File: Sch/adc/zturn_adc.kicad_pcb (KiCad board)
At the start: 4 copper layers, 91.5 x 80 mm, 118 parts, among them CN1 SMA, CN2 SMA, CN3 AudioJack, J1 JP4, J2 Header5, J3 JP2, J4 JP2, J5 JP2, J6 JP2, P1 CONN_02X40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

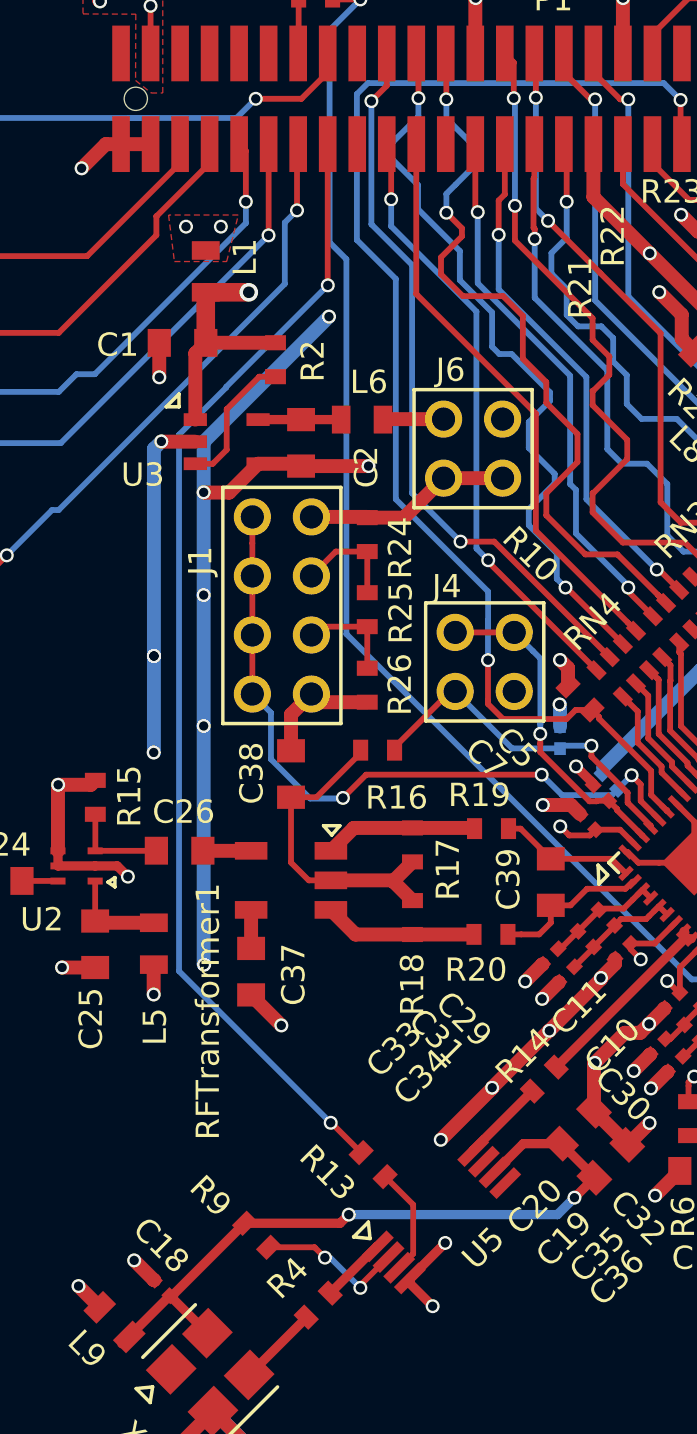
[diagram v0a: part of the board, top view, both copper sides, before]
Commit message: Modify footprint for CDCLVC1102. Changed width of ADC_CLK.
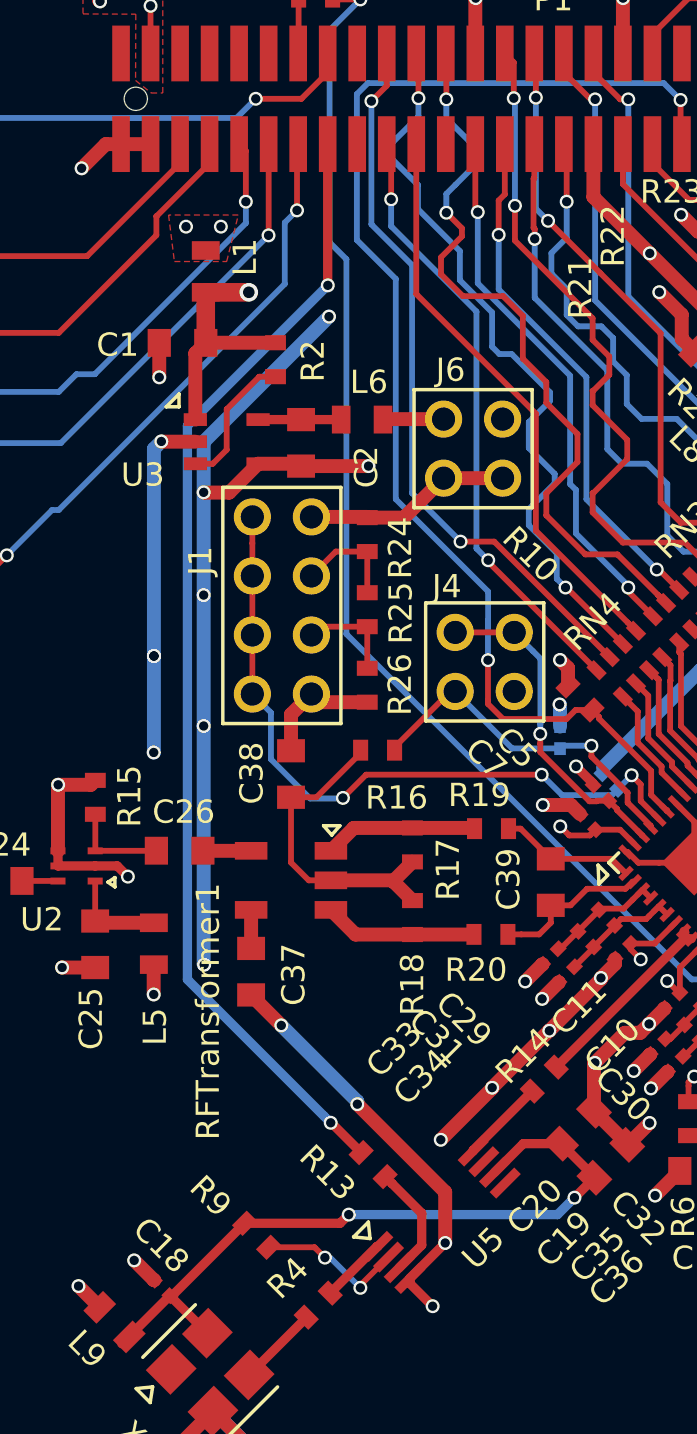
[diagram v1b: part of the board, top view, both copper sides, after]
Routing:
- net GND: track 282.3 -> 294.6 mm, vias 67 -> 68
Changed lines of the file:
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@@
     (thickness 1.6)
     (drawings 7)
-    (tracks 1227)
+    (tracks 1232)
     (zones 0)
     (modules 118)
@@
   (layers
     (0 F.Cu signal)
-    (1 In1.Cu power)
-    (2 In2.Cu power)
+    (1 In1.Cu power hide)
+    (2 In2.Cu power hide)
     (31 B.Cu signal)
     (32 B.Adhes user)
@@
     (add_net /RF_in/VCMA)
     (add_net /RF_in/VCMB)
-    (add_net ADC_CLK)
     (add_net BCLK)
     (add_net DACIN)
@@
     (add_net "Net-(P1-Pad78)")
     (add_net "Net-(P1-Pad79)")
-    (add_net "Net-(R13-Pad2)")
     (add_net "Net-(R2-Pad2)")
     (add_net "Net-(R23-Pad1)")
@@
     (uvia_drill 0.1)
     (add_net /RF_in/CLK40M)
+    (add_net ADC_CLK)
     (add_net "Net-(C12-Pad1)")
     (add_net "Net-(C18-Pad1)")
     (add_net "Net-(C2-Pad1)")
     (add_net "Net-(C49-Pad1)")
+    (add_net "Net-(R13-Pad2)")
     (add_net "Net-(R14-Pad2)")
     (add_net "Net-(R4-Pad1)")
@@
       (net 16 "Net-(C18-Pad1)"))
   )
-  (module adc_lib:CDCLVC1102 (layer F.Cu)
-    (at 129.991951 111.505513 45)
-    (attr smd)
-    (fp_text reference U5 (at 0.254 2.286 45) (layer F.SilkS)
-      (effects (font (size 1 1) (thickness 0.15)))
-    )
-    (fp_text value CDCLVC1102 (at 0.2 -3.45 45) (layer F.Fab)
-      (effects (font (size 1 1) (thickness 0.15)))
-    )
-    (fp_line (start -3.35 -2) (end -2.9 -1.45) (layer F.SilkS) (width 0.15))
-    (fp_line (start -2.45 -2) (end -3.35 -2) (layer F.SilkS) (width 0.15))
-    (fp_line (start -2.9 -1.45) (end -2.45 -2) (layer F.SilkS) (width 0.15))
-    (pad 1 smd rect (at -2.9 -0.975 45) (size 1.5 0.45) (layers F.Cu F.Paste F.Mask)
-      (net 108 "Net-(R4-Pad1)"))
-    (pad 2 smd rect (at -2.9 -0.325 45) (size 1.5 0.45) (layers F.Cu F.Paste F.Mask)
-      (net 110 "Net-(R9-Pad2)"))
-    (pad 3 smd rect (at -2.9 0.325 45) (size 1.5 0.45) (layers F.Cu F.Paste F.Mask)
-      (net 113 "Net-(R13-Pad2)"))
-    (pad 4 smd rect (at -2.9 0.975 45) (size 1.5 0.45) (layers F.Cu F.Paste F.Mask)
-      (net 2 GND))
-    (pad 5 smd rect (at 2.9 0.975 45) (size 1.5 0.45) (layers F.Cu F.Paste F.Mask)
-      (net 158 "Net-(U5-Pad5)"))
-    (pad 6 smd rect (at 2.9 0.325 45) (size 1.5 0.45) (layers F.Cu F.Paste F.Mask)
-      (net 16 "Net-(C18-Pad1)"))
-    (pad 7 smd rect (at 2.9 -0.325 45) (size 1.5 0.45) (layers F.Cu F.Paste F.Mask)
-      (net 159 "Net-(U5-Pad7)"))
-    (pad 8 smd rect (at 2.9 -0.975 45) (size 1.5 0.45) (layers F.Cu F.Paste F.Mask)
-      (net 114 "Net-(R14-Pad2)"))
-  )
   (module adc_lib:MABAES0060 (layer F.Cu)
     (at 123.517281 97.121151 270)
@@
       (net 3 "Net-(C2-Pad1)"))
   )
+  (module adc_lib:CDCLVC1102 (layer F.Cu)
+    (at 129.991951 111.505513 45)
+    (attr smd)
+    (fp_text reference U5 (at 0.254 2.286 45) (layer F.SilkS)
+      (effects (font (size 1 1) (thickness 0.15)))
+    )
+    (fp_text value CDCLVC1102 (at 0.2 -3.45 45) (layer F.Fab)
+      (effects (font (size 1 1) (thickness 0.15)))
+    )
+    (fp_line (start -3.35 -2) (end -2.9 -1.45) (layer F.SilkS) (width 0.15))
+    (fp_line (start -2.45 -2) (end -3.35 -2) (layer F.SilkS) (width 0.15))
+    (fp_line (start -2.9 -1.45) (end -2.45 -2) (layer F.SilkS) (width 0.15))
+    (pad 1 smd rect (at -2.9 -0.975 45) (size 1.5 0.4) (layers F.Cu F.Paste F.Mask)
+      (net 108 "Net-(R4-Pad1)"))
+    (pad 2 smd rect (at -2.9 -0.325 45) (size 1.5 0.4) (layers F.Cu F.Paste F.Mask)
+      (net 110 "Net-(R9-Pad2)"))
+    (pad 3 smd rect (at -2.9 0.325 45) (size 1.5 0.4) (layers F.Cu F.Paste F.Mask)
+      (net 113 "Net-(R13-Pad2)"))
+    (pad 4 smd rect (at -2.9 0.975 45) (size 1.5 0.4) (layers F.Cu F.Paste F.Mask)
+      (net 2 GND))
+    (pad 5 smd rect (at 2.9 0.975 45) (size 1.5 0.4) (layers F.Cu F.Paste F.Mask)
+      (net 158 "Net-(U5-Pad5)"))
+    (pad 6 smd rect (at 2.9 0.325 45) (size 1.5 0.4) (layers F.Cu F.Paste F.Mask)
+      (net 16 "Net-(C18-Pad1)"))
+    (pad 7 smd rect (at 2.9 -0.325 45) (size 1.5 0.4) (layers F.Cu F.Paste F.Mask)
+      (net 159 "Net-(U5-Pad7)"))
+    (pad 8 smd rect (at 2.9 -0.975 45) (size 1.5 0.4) (layers F.Cu F.Paste F.Mask)
+      (net 114 "Net-(R14-Pad2)"))
+  )
   (dimension 80 (width 0.3) (layer Dwgs.User)
     (gr_text "80.000 mm" (at 181.85 95 270) (layer Dwgs.User)
@@
   (segment (start 149.455065 96.833313) (end 150.360876 97.739124) (width 0.25) (layer F.Cu) (net 1))
   (segment (start 122.845 74) (end 122.85 73.995) (width 0.25) (layer F.Cu) (net 1))
+  (segment (start 126.37 106.75) (end 126.37 106.63) (width 0.6) (layer B.Cu) (net 2))
+  (segment (start 126.37 106.63) (end 123.1 103.36) (width 0.6) (layer B.Cu) (net 2))
+  (segment (start 130.15 112.72) (end 130.15 110.53) (width 0.6) (layer F.Cu) (net 2))
+  (segment (start 130.15 110.53) (end 126.37 106.75) (width 0.6) (layer F.Cu) (net 2))
+  (via (at 126.37 106.75) (size 0.6) (drill 0.4) (layers F.Cu B.Cu) (net 2))
   (segment (start 117.62 87.47) (end 117.62 91.61) (width 0.6) (layer B.Cu) (net 2))
   (via (at 117.61 91.62) (size 0.6) (drill 0.4) (layers F.Cu B.Cu) (net 2))
@@
   (segment (start 125.095 62.37) (end 123.965 63.5) (width 0.25) (layer F.Cu) (net 55))
   (segment (start 125.095 61.55) (end 125.095 60.73) (width 0.25) (layer F.Cu) (net 55))
-  (segment (start 125.225 107.55) (end 125.25 107.55) (width 0.25) (layer F.Cu) (net 56))
-  (segment (start 125.25 107.55) (end 126.533812 108.833812) (width 0.25) (layer F.Cu) (net 56))
-  (segment (start 118.7 77.95) (end 118.7 101.025) (width 0.25) (layer B.Cu) (net 56))
-  (segment (start 118.7 101.025) (end 125.225 107.55) (width 0.25) (layer B.Cu) (net 56))
+  (segment (start 125.225 107.55) (end 125.25 107.55) (width 0.4) (layer F.Cu) (net 56))
+  (segment (start 125.25 107.55) (end 126.533812 108.833812) (width 0.4) (layer F.Cu) (net 56))
+  (segment (start 125.1 71.525) (end 119.05999 77.56501) (width 0.4) (layer B.Cu) (net 56))
+  (segment (start 119.05999 77.56501) (end 119.05999 101.38499) (width 0.4) (layer B.Cu) (net 56))
+  (segment (start 119.05999 101.38499) (end 124.925001 107.250001) (width 0.4) (layer B.Cu) (net 56))
+  (segment (start 124.925001 107.250001) (end 125.225 107.55) (width 0.4) (layer B.Cu) (net 56))
+  (segment (start 125.095 65.45) (end 125.095 71.52) (width 0.4) (layer F.Cu) (net 56))
+  (segment (start 125.095 71.52) (end 125.1 71.525) (width 0.4) (layer F.Cu) (net 56))
   (via (at 125.225 107.55) (size 0.6) (drill 0.4) (layers F.Cu B.Cu) (net 56))
-  (segment (start 120.729103 75.920897) (end 118.7 77.95) (width 0.25) (layer B.Cu) (net 56))
-  (segment (start 125.1 71.525) (end 120.729103 75.895897) (width 0.25) (layer B.Cu) (net 56))
-  (segment (start 120.729103 75.895897) (end 120.729103 75.920897) (width 0.25) (layer B.Cu) (net 56))
-  (segment (start 125.095 65.45) (end 125.095 71.52) (width 0.25) (layer F.Cu) (net 56))
-  (segment (start 125.095 71.52) (end 125.1 71.525) (width 0.25) (layer F.Cu) (net 56))
   (via (at 125.1 71.525) (size 0.6) (drill 0.4) (layers F.Cu B.Cu) (net 56))
   (segment (start 130.81 82.55) (end 128.725 80.465) (width 0.25) (layer B.Cu) (net 58))
@@
   (segment (start 134.927557 105.155694) (end 140.450069 99.633182) (width 0.4) (layer F.Cu) (net 112))
   (segment (start 140.450069 99.633182) (end 140.739966 99.633182) (width 0.4) (layer F.Cu) (net 112))
-  (segment (start 127.566188 109.866188) (end 128.772191 111.072191) (width 0.25) (layer F.Cu) (net 113))
-  (segment (start 128.772191 111.072191) (end 128.772191 113.184892) (width 0.25) (layer F.Cu) (net 113))
-  (segment (start 128.772191 113.184892) (end 128.171151 113.785932) (width 0.25) (layer F.Cu) (net 113))
+  (segment (start 128.171151 113.785932) (end 129.14 112.817083) (width 0.4) (layer F.Cu) (net 113))
+  (segment (start 129.14 112.817083) (end 129.14 111.44) (width 0.4) (layer F.Cu) (net 113))
+  (segment (start 129.14 111.44) (end 127.866708 110.166708) (width 0.4) (layer F.Cu) (net 113))
+  (segment (start 127.866708 110.166708) (end 127.566188 109.866188) (width 0.4) (layer F.Cu) (net 113))
   (segment (start 131.353132 108.765474) (end 131.353132 108.730119) (width 0.4) (layer F.Cu) (net 114))
   (segment (start 131.353132 108.730119) (end 133.895181 106.18807) (width 0.4) (layer F.Cu) (net 114))

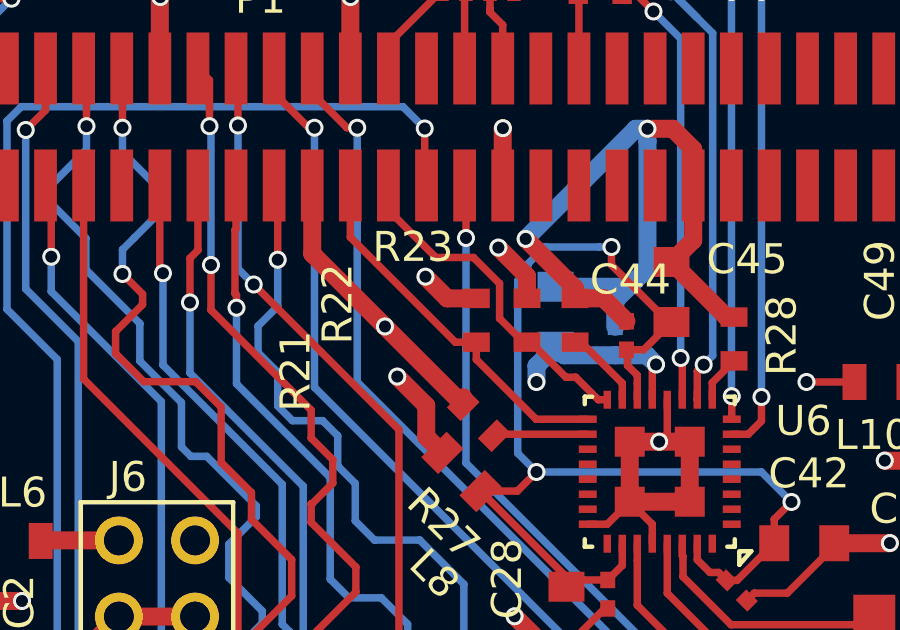
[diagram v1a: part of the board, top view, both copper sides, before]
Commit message: Changed some resistors to 0402.
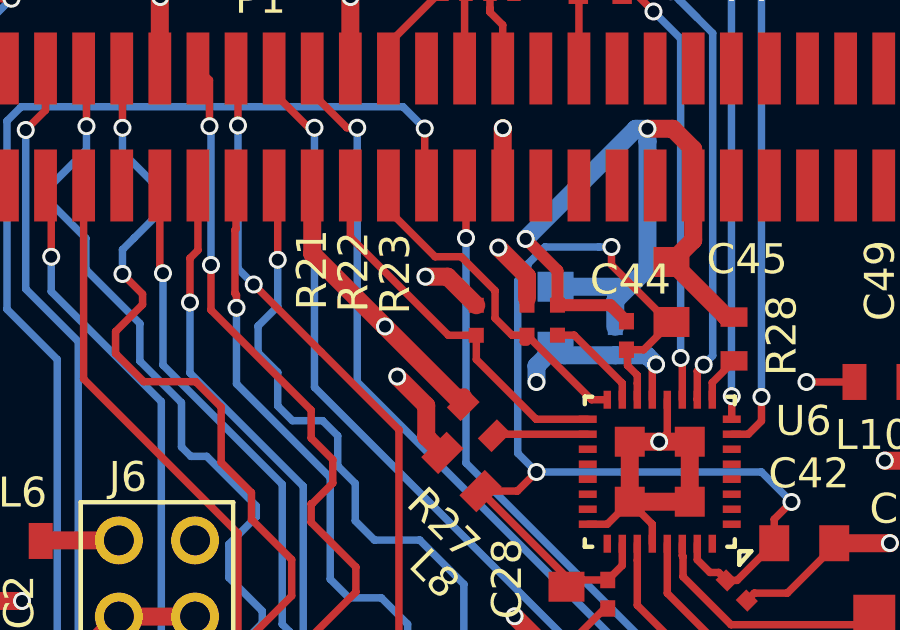
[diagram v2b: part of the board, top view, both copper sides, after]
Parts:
- R21, R22, R23: footprint adc_lib:R0603 -> adc_lib:R0402
- moved R23 0.59 mm to (144.7, 69.9)
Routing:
- net Net-(R23-Pad1): track 2.82 -> 3.37 mm

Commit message: Flipped capacitors around audio DAC
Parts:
- C46, C47: moved to F.Cu
- moved C47 4.47 mm to (149.1, 69.1)
- moved C45 3.26 mm to (145.3, 69.7)
- moved R22 1.31 mm to (143.0, 68.8)
- moved C46 1.23 mm to (147.8, 70.5)
- moved R23 0.87 mm to (143.8, 69.9)
- moved R28 0.76 mm to (151.3, 70.7), turned to 45 degrees
- moved C44 0.39 mm to (146.7, 70.7)
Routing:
- net Net-(C28-Pad1): track 41.2 -> 33.6 mm
- net GND: track 295.1 -> 287.6 mm
- net /AudioDAC/VDDC: track 7.88 -> 6.45 mm, vias 3 -> 2
- net Net-(R23-Pad1): track 3.37 -> 4.54 mm
- net +3V3: track 34.0 -> 32.9 mm

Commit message: Flipped all the parts to the TOP. TODO: change C17,C39 to 0402 size
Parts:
- C4, C40, C53: moved to F.Cu
- moved C40 2.96 mm to (137.4, 92.8), turned to 135 degrees
- moved C53 1.43 mm to (138.7, 93.0), turned to 90 degrees
- moved C8 1.07 mm to (144.7, 103.0), turned to 225 degrees
- moved C4 0.87 mm to (146.4, 102.7)
- moved C6 0.84 mm to (147.7, 102.1), turned to 0 degrees
- moved R10 0.82 mm to (135.3, 88.8), turned to 90 degrees
- moved C7 0.47 mm to (136.4, 95.0), turned to 180 degrees
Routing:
- net GND: track 287.6 -> 282.0 mm
- net /CN/SHDNA: track 55.9 -> 60.3 mm, vias 2 -> 4
- net Net-(C4-Pad1): track 12.7 -> 14.1 mm
- net /CN/MUX: track 60.1 -> 58.9 mm
- net VDD3: track 24.4 -> 23.5 mm
- net /RF_in/VCMA: track 15.1 -> 15.9 mm
- net /RF_in/VCMB: track 26.8 -> 26.1 mm

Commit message: Improve layout
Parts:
- moved C48 4.47 mm to (162.6, 73.8), turned to 0 degrees
- moved C49 2.08 mm to (156.8, 71.1)
- moved L7 1.22 mm to (162.5, 75.8)
- moved L10 1.21 mm to (154.6, 71.2), turned to 270 degrees
- moved C46 0.19 mm to (147.9, 70.7)
- moved C44 0.18 mm to (146.9, 70.7)
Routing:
- net GND: track 282.0 -> 278.2 mm, vias 68 -> 70
- net Net-(C48-Pad1): track 6.99 -> 6.00 mm
- net +3V3: track 32.9 -> 33.8 mm, vias 13 -> 14
- net /AudioDAC/VDDC: track 6.45 -> 5.92 mm

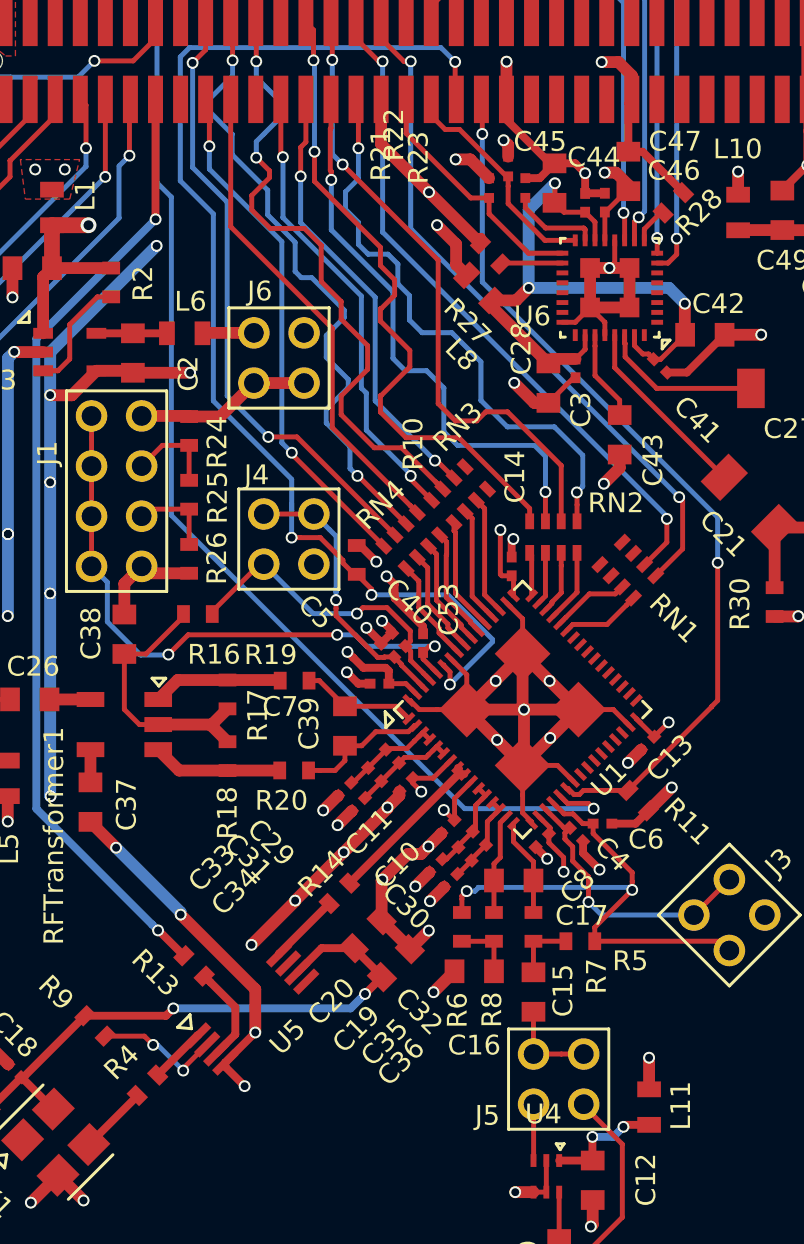
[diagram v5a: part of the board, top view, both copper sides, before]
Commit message: Modify power plane
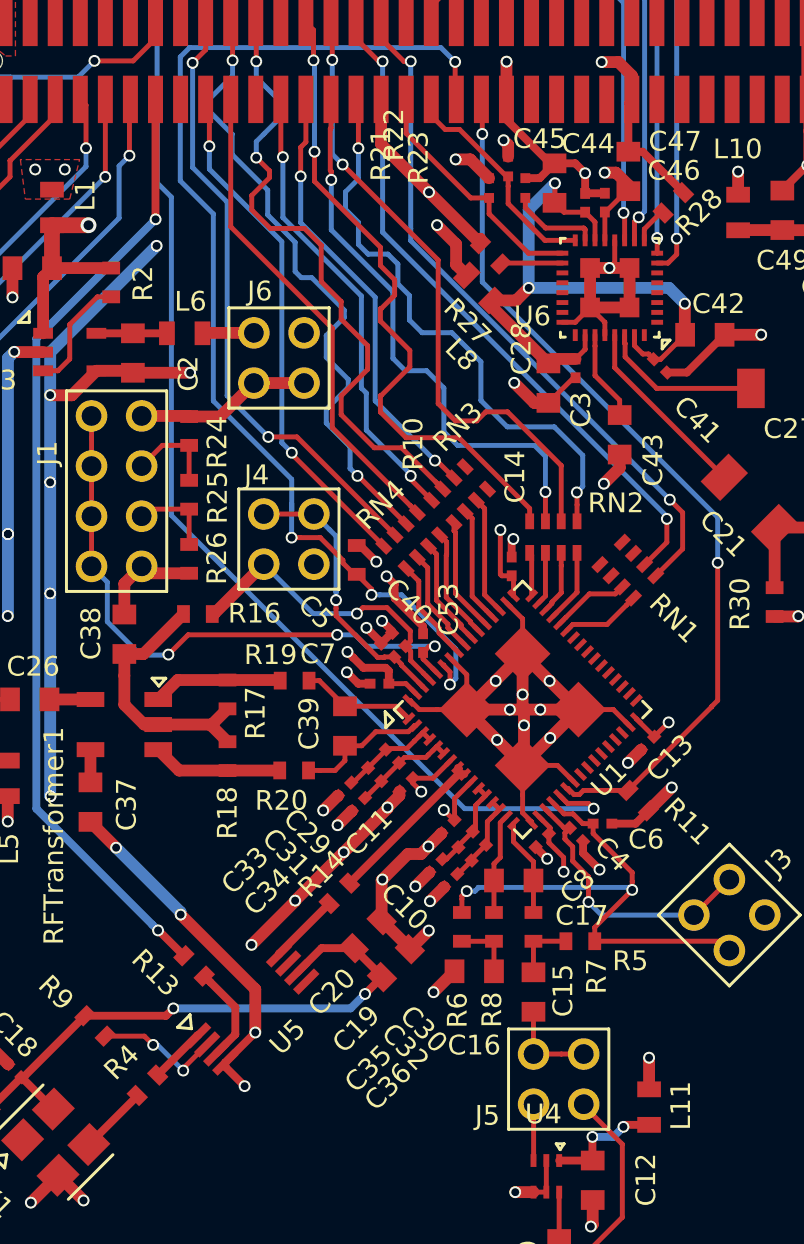
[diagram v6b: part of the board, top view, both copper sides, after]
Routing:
- net /CN/SHDNA: track 60.3 -> 57.4 mm
- net GND: vias 70 -> 73
